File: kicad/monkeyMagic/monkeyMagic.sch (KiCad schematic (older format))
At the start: 67 parts, among them IC3 74LS03

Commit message: A MAME part library is born & some further Monkey Magic work.
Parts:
- removed D4: DIODE, ~, symbol DIODE
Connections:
- net at R1.1: now also R2.1, R3.1, R4.1, R5.1, R6.1, R7.1, R8.1
- net at R1.2: now also D1.1 (A)
- net at R2.2: now also D2.1 (A)
- net at R3.2: now also D3.1 (A)
- net at R4.2: now also D4.1 (A)
- net at R5.2: now also D5.1 (A)
- net at R6.2: now also D6.1 (A)
- net at R7.2: now also D7.1 (A)
- net at R8.2: now also D8.1 (A)
- net at R9.2: now also D12.1 (A)
- net at R10.2: now also D11.1 (A)
- net at R11.2: now also D10.1 (A)
- net at R12.2: now also D9.1 (A)
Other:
- moved on the sheet: C1, C10, C11, C12, C14, C2, C3, C4, C5, C6, C7, D1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

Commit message: Nearly fully-wired now.
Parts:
- added IC?: SN74123, ~, symbol SN74123
- added IC?: SN76477, ~, symbol SN76477
- added IC?: M53242, ~, symbol M53242
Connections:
- net labels added: GND, HELLO, VCC
- wire segments 21 -> 388
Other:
- note added: "Disconnected on our MMagic"
- note added: "Pin 14"
- note added: "Pin 7"
- note added: "Resistor Array"
- note added: "Resistor\nArray\nOf Some\nSort"
- note added: "Trace #1"
- note added: "Trace #10"
- note added: "Trace #11"
- note added: "Trace #12"
- note added: "Trace #13"
- note added: "Trace #14\n"
- note added: "Trace #15"
- note added: "Trace #16"
- note added: "Trace #17"
- note added: "Trace #18"
- note added: "Trace #2"
- note added: "Trace #21"
- note added: "Trace #22"
- note added: "Trace #23"
- note added: "Trace #25"
- note added: "Trace #26"
- note added: "Trace #27"
- note added: "Trace #28"
- note added: "Trace #3"
- note added: "Trace #31"
- note added: "Trace #32"
- note added: "Trace #33"
- note added: "Trace #34"
- note added: "Trace #35"
- note added: "Trace #36 ****"
- note added: "Trace #38"
- note added: "Trace #39"
- note added: "Trace #40"
- note added: "Trace #41"
- note added: "Trace #42"
- note added: "Trace #43"
- note added: "Trace #44\n"
- note added: "Trace #45\n"
- note added: "Trace #46\n"
- note added: "Trace #5"
- note added: "Trace #6"
- note added: "Trace #7"
- note added: "Trace #8"
- note added: "Trace #9"
- note added: "VR1?"
- moved on the sheet: C1, C10, C11, C12, C14, C2, C3, C4, C5, C6, C7, D1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

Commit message: Added input connector to MAME.lib & finished up connections in Monkey Magic.
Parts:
- added I_2, I_3, I_4, I_5, I_POT: 0, symbol CONN_01X01
- added VR1: POT, ~, symbol POT
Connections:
- net labels added: STV
- net labels removed: VCC
- wire segments 388 -> 384
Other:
- note added: "Hooked up correctly?"
- note added: "Resistor \nArray 102\n(1k)"
- note added: "Resistor\nArray 102\n(1k)"
- note removed: "Resistor Array"
- note removed: "Resistor\nArray\nOf Some\nSort"
- note removed: "VR1?"
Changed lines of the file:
@@
 Sheet 1 1
 Title "Monkey Magic Sound Board"
-Date "17 jun 2015"
+Date "18 jun 2015"
 Rev ""
 Comp "Nintendo"
@@
 Text Notes 3250 11150 0    60   ~ 0
 Trace #23
-Text Notes 2450 10950 0    60   ~ 0
-Resistor\nArray\nOf Some\nSort
-Text Notes 13250 1700 0    60   ~ 0
-Resistor Array
+Text Notes 13450 1350 0    60   ~ 0
+Resistor \nArray 102\n(1k)
 Text Notes 13300 3950 0    60   ~ 0
 Trace #25
@@
 Text Notes 8350 5100 0    60   ~ 0
 Trace #28
-Text Notes 19350 4850 0    60   ~ 0
-VR1?
 Text Notes 17350 3550 0    60   ~ 0
 Trace #34
@@
 Text Notes 11150 7200 0    60   ~ 0
 Disconnected on our MMagic
-$Comp
-L VCC #PWR01
-U 1 1 5581E4CD
-P 5150 1150
-F 0 "#PWR01" H 5150 1250 30  0001 C CNN
-F 1 "VCC" H 5150 1250 30  0000 C CNN
-F 2 "" H 5150 1150 60  0000 C CNN
-F 3 "" H 5150 1150 60  0000 C CNN
-	1    5150 1150
-	1    0    0    -1
-$EndComp
 $Comp
 L GND #PWR02
@@
 Text Notes 3300 1150 0    60   ~ 0
 Trace #1
+Text Notes 5950 4300 0    60   ~ 0
+Pin 7
+Text Notes 6600 950  0    60   ~ 0
+Trace #2
+Text Notes 1350 11050 0    60   ~ 0
+Resistor\nArray 102\n(1k)
+$Comp
+L CONN_01X01 I_3
+U 1 1 55828715
+P 550 10950
+F 0 "I_3" H 550 11050 50  0000 C CNN
+F 1 "0" V 650 10950 50  0000 C CNN
+F 2 "" H 550 10950 60  0000 C CNN
+F 3 "" H 550 10950 60  0000 C CNN
+	1    550  10950
+	-1   0    0    1
+$EndComp
+$Comp
+L CONN_01X01 I_4
+U 1 1 55828A59
+P 800 11050
+F 0 "I_4" H 800 11150 50  0000 C CNN
+F 1 "0" V 900 11050 50  0000 C CNN
+F 2 "" H 800 11050 60  0000 C CNN
+F 3 "" H 800 11050 60  0000 C CNN
+	1    800  11050
+	-1   0    0    1
+$EndComp
+$Comp
+L CONN_01X01 I_5
+U 1 1 55828A5F
+P 1050 11150
+F 0 "I_5" H 1050 11250 50  0000 C CNN
+F 1 "0" V 1150 11150 50  0000 C CNN
+F 2 "" H 1050 11150 60  0000 C CNN
+F 3 "" H 1050 11150 60  0000 C CNN
+	1    1050 11150
+	-1   0    0    1
+$EndComp
+$Comp
+L CONN_01X01 I_2
+U 1 1 55828DAC
+P 13550 600
+F 0 "I_2" H 13550 700 50  0000 C CNN
+F 1 "0" V 13650 600 50  0000 C CNN
+F 2 "" H 13550 600 60  0000 C CNN
+F 3 "" H 13550 600 60  0000 C CNN
+	1    13550 600
+	0    -1   -1   0
+$EndComp
+$Comp
+L CONN_01X01 I_POT
+U 1 1 55828FAC
+P 17350 600
+F 0 "I_POT" H 17350 700 50  0000 C CNN
+F 1 "0" V 17450 600 50  0000 C CNN
+F 2 "" H 17350 600 60  0000 C CNN
+F 3 "" H 17350 600 60  0000 C CNN
+	1    17350 600
+	0    -1   -1   0
+$EndComp
+Text GLabel 5050 1050 0    60   Input ~ 0
+STV
 Connection ~ 12600 6700
 Wire Wire Line
@@
 	11500 7350 8150 7350
 Wire Wire Line
-	13550 1550 13550 1300
-Wire Wire Line
-	13550 3950 13550 1800
-Wire Wire Line
-	13100 3950 13550 3950
-Wire Wire Line
-	2350 11150 2150 11150
-Wire Wire Line
-	2350 11050 2150 11050
-Wire Wire Line
-	2350 10950 2150 10950
-Wire Wire Line
-	4200 11150 2950 11150
-Wire Wire Line
-	4200 11050 2950 11050
-Wire Wire Line
-	4200 10950 2950 10950
+	13550 800  13550 3950
+Wire Wire Line
+	13550 3950 13100 3950
+Wire Wire Line
+	1250 11150 4200 11150
+Wire Wire Line
+	1000 11050 4200 11050
+Wire Wire Line
+	750  10950 4200 10950
 Connection ~ 12500 7600
 Wire Wire Line
@@
 	17350 3900 17200 3900
 Wire Wire Line
-	17350 1300 17350 3900
-Wire Wire Line
-	18500 7950 18500 5100
-Wire Wire Line
-	18500 5100 19550 5100
+	17350 800  17350 3900
+Wire Wire Line
+	18500 5000 18500 7950
 Connection ~ 18500 7950
 Wire Wire Line
@@
 Wire Wire Line
 	16500 4150 19450 4150
-Wire Wire Line
-	19450 4150 19450 4650
-Wire Wire Line
-	19550 5100 19550 4950
 Wire Notes Line
 	11550 7250 12250 7250
@@
 	7200 4300 6250 4300
 Connection ~ 7200 950
-Text Notes 5950 4300 0    60   ~ 0
-Pin 7
 Wire Wire Line
 	1850 950  1850 10850
@@
 	6000 10200 1950 10200
 Connection ~ 1950 10200
-Text Notes 6600 950  0    60   ~ 0
-Trace #2
 Wire Wire Line
 	20450 9050 17550 9050
 Connection ~ 20450 8750
-Wire Wire Line
-	19350 4950 19350 5000
-Wire Wire Line
-	19350 5000 20450 5000
 Connection ~ 20450 5000
+Wire Notes Line
+	1300 10900 1300 11300
+Wire Notes Line
+	2400 11200 2950 11200
+Wire Notes Line
+	1850 11300 1850 10900
+Wire Notes Line
+	1850 10900 1300 10900
+Wire Notes Line
+	13400 1250 13400 1550
+Wire Notes Line
+	13400 1550 13900 1550
+Wire Notes Line
+	13900 1550 13900 1250
+Wire Notes Line
+	13900 1250 13400 1250
+Wire Wire Line
+	5050 1050 5150 1050
+Wire Wire Line
+	5150 1050 5150 1150
+Wire Wire Line
+	19700 5000 20450 5000
+Wire Wire Line
+	18500 5000 19200 5000
+Wire Wire Line
+	19450 4150 19450 4850
+$Comp
+L POT VR1
+U 1 1 558296D7
+P 19450 5000
+F 0 "VR1" H 19450 4900 50  0000 C CNN
+F 1 "POT" H 19450 5000 50  0000 C CNN
+F 2 "~" H 19450 5000 60  0000 C CNN
+F 3 "~" H 19450 5000 60  0000 C CNN
+	1    19450 5000
+	1    0    0    -1
+$EndComp
+Wire Notes Line
+	19100 4750 19100 5150
+Wire Notes Line
+	19100 5150 19750 5150
+Wire Notes Line
+	19750 5150 19750 4750
+Wire Notes Line
+	19750 4750 19100 4750
+Text Notes 18950 5250 0    60   ~ 0
+Hooked up correctly?
+Wire Notes Line
+	1300 11300 1850 11300
 $EndSCHEMATC

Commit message: Greatly cleans up STV connections.  Sanity is 50% restored
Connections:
- net GND: now also IC?.8 (PIN8)
- net STV: no longer IC?.8 (PIN8)
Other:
- note added: "Trace #36"
- note removed: "Trace #36 ****"
- moved on the sheet: R25
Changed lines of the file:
@@
 L R R25
 U 1 1 558129ED
-P 15250 9800
-F 0 "R25" V 15330 9800 40  0000 C CNN
-F 1 "20k" V 15257 9801 40  0000 C CNN
-F 2 "~" V 15180 9800 30  0000 C CNN
-F 3 "~" H 15250 9800 30  0000 C CNN
-	1    15250 9800
+P 16300 9800
+F 0 "R25" V 16380 9800 40  0000 C CNN
+F 1 "20k" V 16307 9801 40  0000 C CNN
+F 2 "~" V 16230 9800 30  0000 C CNN
+F 3 "~" H 16300 9800 30  0000 C CNN
+	1    16300 9800
 	0    1    1    0
 $EndComp
@@
 Trace #38
 Text Notes 17700 7950 0    60   ~ 0
-Trace #36 ****
+Trace #36
 Text Notes 13950 7500 0    60   ~ 0
 Trace #46\n
@@
 Text Notes 5250 6600 0    60   ~ 0
 Pin 14
-Text Notes 3300 1150 0    60   ~ 0
+Text Notes 3400 6550 0    60   ~ 0
 Trace #1
 Text Notes 5950 4300 0    60   ~ 0
@@
 	0    -1   -1   0
 $EndComp
-Text GLabel 5050 1050 0    60   Input ~ 0
+Text GLabel 3150 6550 0    60   Input ~ 0
 STV
+$Comp
+L POT VR1
+U 1 1 558296D7
+P 19450 5000
+F 0 "VR1" H 19450 4900 50  0000 C CNN
+F 1 "POT" H 19450 5000 50  0000 C CNN
+F 2 "~" H 19450 5000 60  0000 C CNN
+F 3 "~" H 19450 5000 60  0000 C CNN
+	1    19450 5000
+	1    0    0    -1
+$EndComp
+Text Notes 18950 5250 0    60   ~ 0
+Hooked up correctly?
+Text GLabel 2900 11250 0    60   Input ~ 0
+STV
+$Comp
+L GND #PWR?
+U 1 1 55829C36
+P 6000 10000
+F 0 "#PWR?" H 6000 10000 30  0001 C CNN
+F 1 "GND" H 6000 9930 30  0001 C CNN
+F 2 "" H 6000 10000 60  0000 C CNN
+F 3 "" H 6000 10000 60  0000 C CNN
+	1    6000 10000
+	1    0    0    1
+$EndComp
+Text GLabel 21550 9150 2    60   Input ~ 0
+STV
+Text Notes 2900 11250 0    60   ~ 0
+Trace #1
+Text Notes 21100 9150 0    60   ~ 0
+Trace #1
+Text GLabel 9600 4300 0    60   Input ~ 0
+STV
+Text Notes 10050 4300 0    60   ~ 0
+Trace #1
+Text GLabel 14500 3500 0    60   Input ~ 0
+STV
+Text Notes 14550 3500 0    60   ~ 0
+Trace #1
 Connection ~ 12600 6700
 Wire Wire Line
@@
 	13400 9800 14900 9800
 Wire Wire Line
-	14900 9800 15000 9800
+	14900 9800 16050 9800
 Wire Wire Line
 	15800 12750 15500 12750
@@
 	11550 7450 11550 7250
 Wire Wire Line
-	1950 1150 5150 1150
-Wire Wire Line
-	5150 1150 10900 1150
-Wire Wire Line
-	10900 1150 13200 1150
-Wire Wire Line
-	13200 1150 15150 1150
-Wire Wire Line
-	1950 1150 1950 6600
-Wire Wire Line
-	1950 6600 1950 10200
-Wire Wire Line
-	1950 10200 1950 11250
-Wire Wire Line
-	1950 11250 1950 14800
-Wire Wire Line
-	1950 14800 21050 14800
-Wire Wire Line
-	21050 14800 21050 9150
-Wire Wire Line
-	21050 9150 17950 9150
-Wire Wire Line
-	17950 9150 17550 9150
-Wire Wire Line
-	4200 11250 1950 11250
-Connection ~ 1950 11250
-Wire Wire Line
-	1950 6600 5150 6600
-Connection ~ 1950 6600
-Wire Wire Line
-	15150 1150 15150 3350
-Wire Wire Line
-	15150 3350 15150 3700
-Wire Wire Line
-	15150 3350 15400 3350
-Connection ~ 5150 1150
-Wire Wire Line
-	11000 4050 10900 4050
-Wire Wire Line
-	10900 4050 10900 1150
-Connection ~ 10900 1150
-Wire Wire Line
-	13100 3850 13200 3850
-Wire Wire Line
-	13200 4600 13200 4350
-Wire Wire Line
-	13200 4350 13200 3850
-Wire Wire Line
-	13200 3850 13200 1150
-Connection ~ 13200 1150
-Wire Wire Line
-	11950 4600 12400 4600
-Wire Wire Line
-	12400 4600 13200 4600
-Wire Wire Line
-	13200 4600 13550 4600
-Wire Wire Line
-	13550 4600 14850 4600
-Wire Wire Line
-	14850 4600 15200 4600
-Connection ~ 13200 3850
-Wire Wire Line
-	13800 4350 13200 4350
-Connection ~ 13200 4350
-Wire Wire Line
-	12300 5100 12400 5100
-Wire Wire Line
-	12400 5100 12400 4600
-Connection ~ 12400 4600
-Wire Wire Line
-	14850 4600 14850 4850
-Wire Wire Line
-	14850 4850 14750 4850
-Connection ~ 13200 4600
-Wire Wire Line
-	15200 4600 15200 5150
-Wire Wire Line
-	15200 5150 15600 5150
-Connection ~ 14850 4600
+	17550 9150 17950 9150
+Wire Wire Line
+	17950 9150 21550 9150
+Wire Wire Line
+	10700 4050 11000 4050
 Wire Wire Line
 	13650 7850 13550 7850
 Wire Wire Line
-	13550 7850 13550 4600
-Connection ~ 13550 4600
-Wire Wire Line
-	15500 9800 17950 9800
+	16550 9800 17950 9800
 Wire Wire Line
 	17950 9800 17950 9150
 Connection ~ 17950 9150
 Wire Wire Line
-	15150 3700 15400 3700
-Connection ~ 15150 3350
+	15000 3700 15400 3700
 Wire Wire Line
 	6350 900  6350 950
@@
 Connection ~ 6350 950
 Wire Wire Line
-	5900 10550 6000 10550
-Wire Wire Line
-	6000 10550 6000 10200
-Wire Wire Line
-	6000 10200 1950 10200
-Connection ~ 1950 10200
+	6000 10550 5900 10550
+Wire Wire Line
+	6000 10000 6000 10550
 Wire Wire Line
 	20450 9050 17550 9050
@@
 Wire Notes Line
 	1300 10900 1300 11300
-Wire Notes Line
-	2400 11200 2950 11200
 Wire Notes Line
 	1850 11300 1850 10900
@@
 	13900 1250 13400 1250
 Wire Wire Line
-	5050 1050 5150 1050
-Wire Wire Line
-	5150 1050 5150 1150
-Wire Wire Line
 	19700 5000 20450 5000
 Wire Wire Line
@@
 Wire Wire Line
 	19450 4150 19450 4850
-$Comp
-L POT VR1
-U 1 1 558296D7
-P 19450 5000
-F 0 "VR1" H 19450 4900 50  0000 C CNN
-F 1 "POT" H 19450 5000 50  0000 C CNN
-F 2 "~" H 19450 5000 60  0000 C CNN
-F 3 "~" H 19450 5000 60  0000 C CNN
-	1    19450 5000
-	1    0    0    -1
-$EndComp
 Wire Notes Line
 	19100 4750 19100 5150
@@
 Wire Notes Line
 	19750 4750 19100 4750
-Text Notes 18950 5250 0    60   ~ 0
-Hooked up correctly?
 Wire Notes Line
 	1300 11300 1850 11300
+Wire Wire Line
+	3150 6550 5150 6550
+Wire Wire Line
+	2900 11250 4200 11250
+Wire Wire Line
+	10700 4050 10700 4300
+Wire Wire Line
+	10700 4300 9600 4300
+Wire Wire Line
+	14500 3500 15000 3500
+Wire Wire Line
+	15000 3350 15000 3500
+Wire Wire Line
+	15000 3500 15000 3700
+Connection ~ 15000 3500
+Wire Wire Line
+	15000 3350 15400 3350
+Text GLabel 14100 6450 2    60   Input ~ 0
+STV
+Text Notes 13650 6450 0    60   ~ 0
+Trace #1
+Wire Wire Line
+	14100 6450 13550 6450
+Wire Wire Line
+	13550 6450 13550 7850
+Wire Wire Line
+	13100 3850 14300 3850
+Text Notes 13850 3850 0    60   ~ 0
+Trace #1
+Text GLabel 14300 3850 2    60   Input ~ 0
+STV
+Text Notes 14050 5300 0    60   ~ 0
+Trace #1
+Text GLabel 14500 5300 2    60   Input ~ 0
+STV
+Wire Wire Line
+	14500 5300 13100 5300
+Wire Wire Line
+	13100 5300 13100 5100
+Wire Wire Line
+	13100 5100 13100 4600
+Wire Wire Line
+	13100 4600 13100 4350
+Wire Wire Line
+	13100 4350 13800 4350
+Wire Wire Line
+	11950 4600 13100 4600
+Connection ~ 13100 4600
+Wire Wire Line
+	12300 5100 13100 5100
+Wire Wire Line
+	13100 5100 14900 5100
+Wire Wire Line
+	14900 5100 15450 5100
+Connection ~ 13100 5100
+Wire Wire Line
+	14900 5100 14900 4850
+Wire Wire Line
+	14900 4850 14750 4850
+Wire Wire Line
+	15450 5100 15450 5150
+Wire Wire Line
+	15450 5150 15600 5150
+Connection ~ 14900 5100
 $EndSCHEMATC

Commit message: Cleaned up ground.  Sanity fully restored.
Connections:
- net GND: now also C1.1, C10.1, C11.1, C12.1, C14.2, C3.2, C4.1, C5.1, C6.2, IC?.1 (1A), IC?.12 (PIN12), IC?.2 (GROUND), IC?.8 (GND), R13.2, R14.1, R18.1, R19.1, R24.1, VR1.3
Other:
- moved on the sheet: I_2, I_POT

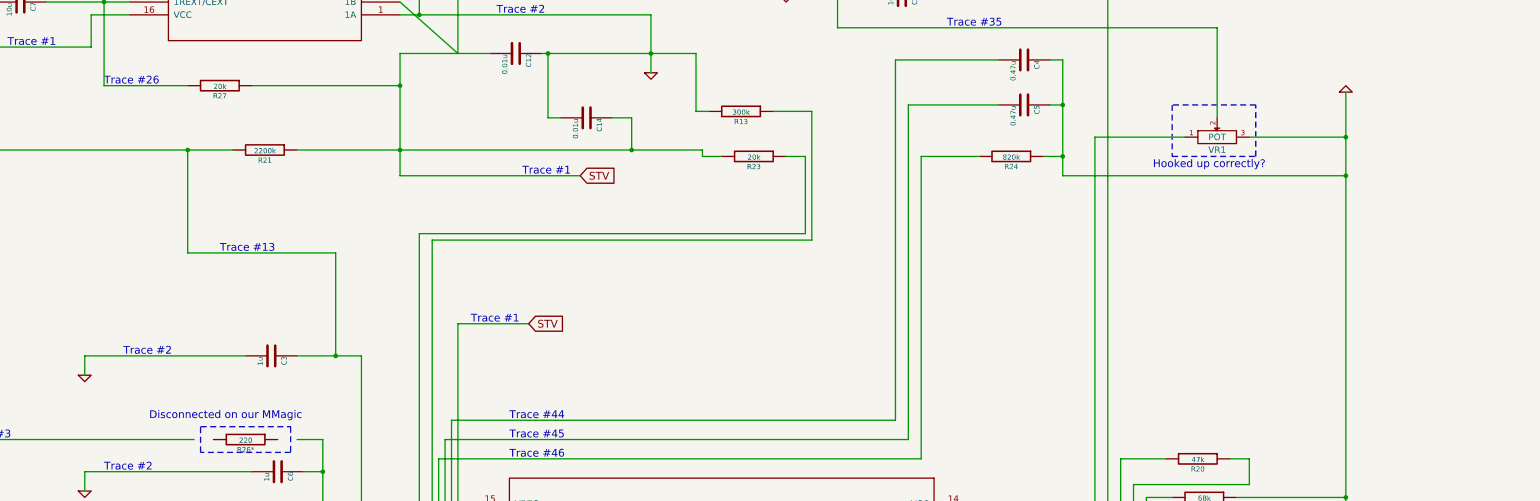
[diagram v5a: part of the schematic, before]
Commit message: Adds a few notes from tests done on the board.
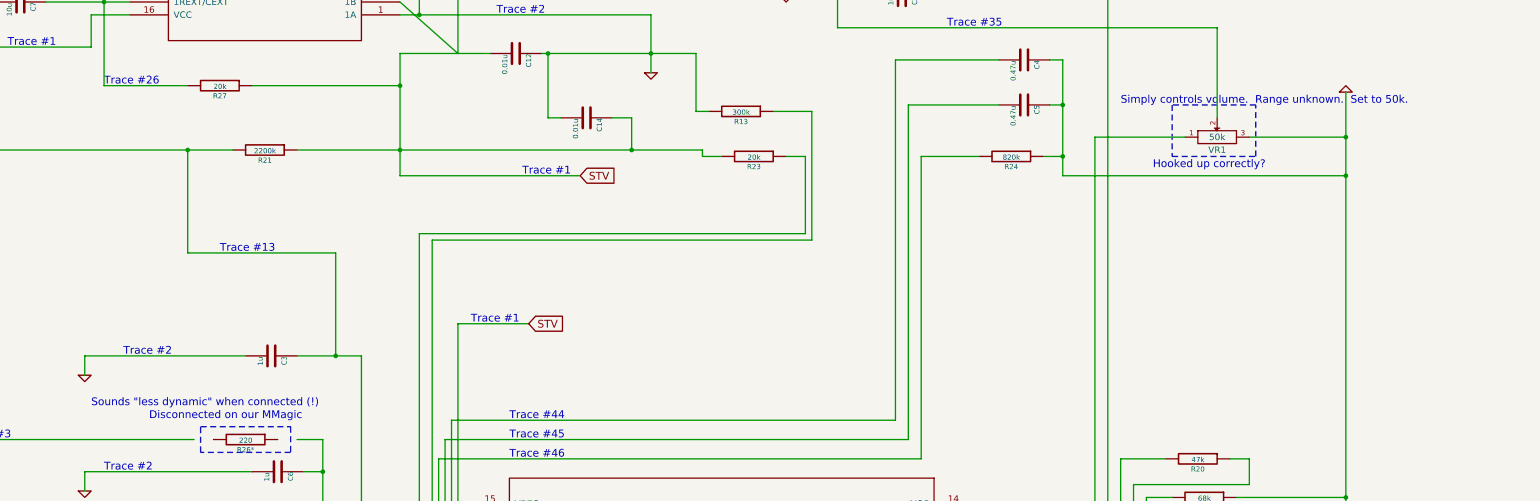
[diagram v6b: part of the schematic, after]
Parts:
- VR1: value POT -> 50k
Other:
- note added: "Simply controls volume. Range unknown. Set to 50k."
- note added: "Sounds "less dynamic" when connected (!)"
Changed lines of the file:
@@
 Sheet 1 1
 Title "Monkey Magic Sound Board"
-Date "18 jun 2015"
+Date "24 jun 2015"
 Rev ""
 Comp "Nintendo"
@@
 P 19450 5000
 F 0 "VR1" H 19450 4900 50  0000 C CNN
-F 1 "POT" H 19450 5000 50  0000 C CNN
+F 1 "50k" H 19450 5000 50  0000 C CNN
 F 2 "~" H 19450 5000 60  0000 C CNN
 F 3 "~" H 19450 5000 60  0000 C CNN
@@
 	1    0    0    1
 $EndComp
+Text Notes 10700 7100 0    60   ~ 0
+Sounds "less dynamic" when connected (!)
+Text Notes 18700 4750 0    60   ~ 0
+Simply controls volume.  Range unknown.  Set to 50k.
 $EndSCHEMATC
